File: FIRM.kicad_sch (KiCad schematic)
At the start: 111 parts, among them J1 Conn_01x02_Pin, J2 DM3CS-SF, Q2 IRLML6402, U1 STM32F405RGTx, U2 MIC5219-3.3YM5, U6 A-USBC-20F0-EA-GSR05, U7 W25Q128JVS, U8 ADXL371, U9 INA219AxDCN, X2 32.768khz, Y1 12 MHz

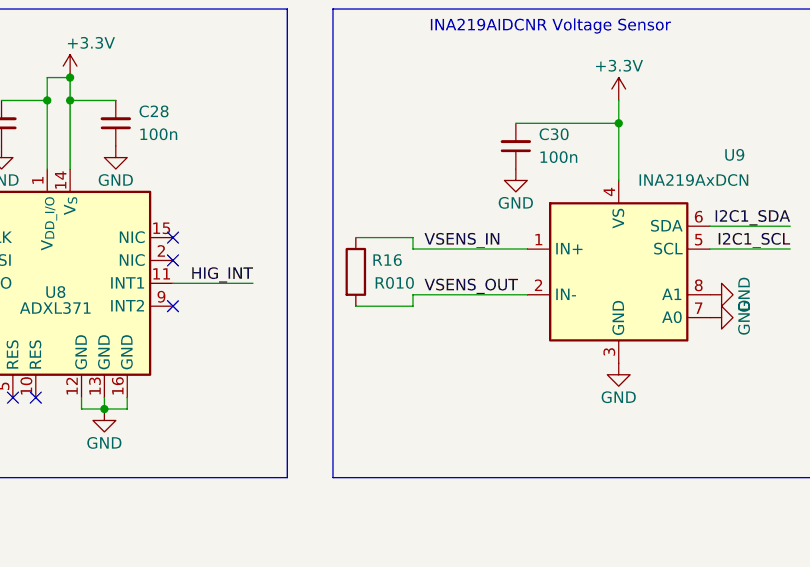
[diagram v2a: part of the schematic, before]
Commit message: Made components 0402s
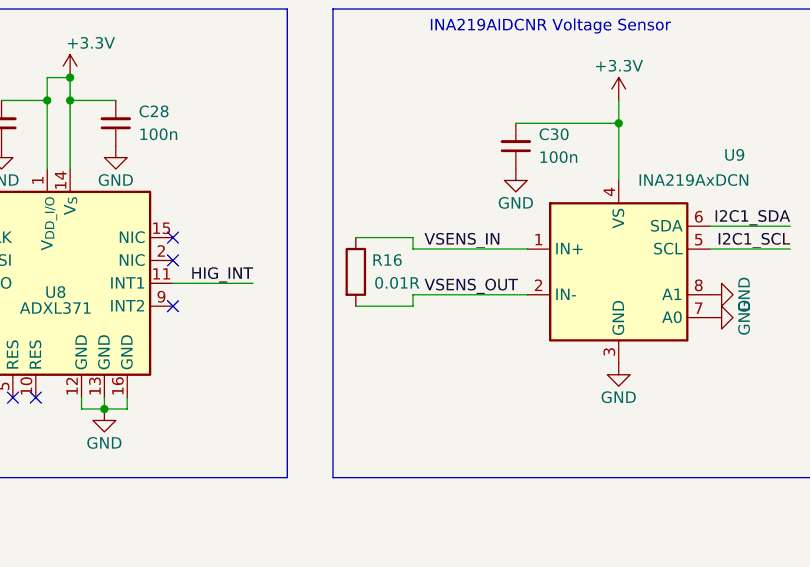
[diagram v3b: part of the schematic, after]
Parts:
- C1, C10, C11, C12, C13, C14, C15, C16, C17, C18, C19, C2, C20, C21, C22, C23, C24, C25, C26, C27, C28, C29, C3, C30, C4, C5, C6, C7, C8, C9: footprint Capacitor_SMD:C_0603_1608Metric -> Capacitor_SMD:C_0402_1005Metric
- D2, D3, D4, D5: footprint LED_SMD:LED_0805_2012Metric -> LED_SMD:LED_0402_1005Metric
- R1, R10, R11, R12, R13, R14, R15, R18, R19, R2, R20, R21, R22, R3, R4, R5, R6, R7, R8, R9: footprint Resistor_SMD:R_0603_1608Metric -> Resistor_SMD:R_0402_1005Metric
- R16: value R010 -> 0.01R; footprint (none) -> Resistor_SMD:R_0402_1005Metric
- U5: footprint Package_LGA:ST_HLGA-10_2x2mm_P0.5mm_LayoutBorder3x2y -> sensors:BMPFootprintNoSolderMask
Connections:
- new net: U8.10 (RES), U8.13 (GND), U8.16 (GND)
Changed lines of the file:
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@@
 			)
 		)
-		(property "Footprint" "Capacitor_SMD:C_0603_1608Metric"
+		(property "Footprint" "Capacitor_SMD:C_0402_1005Metric"
 			(at 88.5952 45.72 0)
 			(effects
@@
 			)
 		)
-		(property "Footprint" "Capacitor_SMD:C_0603_1608Metric"
+		(property "Footprint" "Capacitor_SMD:C_0402_1005Metric"
 			(at 37.7952 45.72 0)
 			(effects
@@
 			)
 		)
-		(property "Footprint" "Resistor_SMD:R_0603_1608Metric"
+		(property "Footprint" "Resistor_SMD:R_0402_1005Metric"
 			(at 21.082 255.27 90)
 			(effects
@@
 			)
 		)
-		(property "Footprint" "Resistor_SMD:R_0603_1608Metric"
+		(property "Footprint" "Resistor_SMD:R_0402_1005Metric"
 			(at 28.702 66.04 90)
 			(effects
@@
 			)
 		)
-		(property "Footprint" "Capacitor_SMD:C_0603_1608Metric"
+		(property "Footprint" "Capacitor_SMD:C_0402_1005Metric"
 			(at 340.36 224.79 0)
 			(effects
@@
 			)
 		)
-		(property "Footprint" "Capacitor_SMD:C_0603_1608Metric"
+		(property "Footprint" "Capacitor_SMD:C_0402_1005Metric"
 			(at 20.0152 64.77 0)
 			(effects
@@
 			)
 		)
-		(property "Footprint" "Capacitor_SMD:C_0603_1608Metric"
+		(property "Footprint" "Capacitor_SMD:C_0402_1005Metric"
 			(at 285.75 105.41 0)
 			(effects
@@
 			)
 		)
-		(property "Footprint" "Resistor_SMD:R_0603_1608Metric"
+		(property "Footprint" "Resistor_SMD:R_0402_1005Metric"
 			(at 52.07 177.8 0)
 			(effects
@@
 			)
 		)
-		(property "Footprint" "LED_SMD:LED_0805_2012Metric"
+		(property "Footprint" "LED_SMD:LED_0402_1005Metric"
 			(at 191.77 116.84 0)
 			(effects
@@
 			)
 		)
-		(property "Footprint" "Capacitor_SMD:C_0603_1608Metric"
+		(property "Footprint" "Capacitor_SMD:C_0402_1005Metric"
 			(at 64.77 195.58 0)
 			(effects
@@
 			)
 		)
-		(property "Footprint" "Resistor_SMD:R_0603_1608Metric"
+		(property "Footprint" "Resistor_SMD:R_0402_1005Metric"
 			(at 59.69 177.8 0)
 			(effects
@@
 			)
 		)
-		(property "Footprint" "Resistor_SMD:R_0603_1608Metric"
+		(property "Footprint" "Resistor_SMD:R_0402_1005Metric"
 			(at 25.4 177.8 0)
 			(effects
@@
 			)
 		)
-		(property "Footprint" "Resistor_SMD:R_0603_1608Metric"
+		(property "Footprint" "Resistor_SMD:R_0402_1005Metric"
 			(at 153.67 111.76 0)
 			(effects
@@
 			)
 		)
-		(property "Footprint" "Resistor_SMD:R_0603_1608Metric"
+		(property "Footprint" "Resistor_SMD:R_0402_1005Metric"
 			(at 38.1 212.09 0)
 			(effects
@@
 			)
 		)
-		(property "Footprint" "Capacitor_SMD:C_0603_1608Metric"
+		(property "Footprint" "Capacitor_SMD:C_0402_1005Metric"
 			(at 66.04 240.03 0)
 			(effects
@@
 			)
 		)
-		(property "Footprint" "Capacitor_SMD:C_0603_1608Metric"
+		(property "Footprint" "Capacitor_SMD:C_0402_1005Metric"
 			(at 228.6 102.87 0)
 			(effects
@@
 			)
 		)
-		(property "Footprint" "Capacitor_SMD:C_0603_1608Metric"
+		(property "Footprint" "Capacitor_SMD:C_0402_1005Metric"
 			(at 42.8752 92.71 0)
 			(effects
@@
 			)
 		)
-		(property "Footprint" "Capacitor_SMD:C_0603_1608Metric"
+		(property "Footprint" "Capacitor_SMD:C_0402_1005Metric"
 			(at 143.2052 45.72 0)
 			(effects
@@
 			)
 		)
-		(property "Footprint" "LED_SMD:LED_0805_2012Metric"
+		(property "Footprint" "LED_SMD:LED_0402_1005Metric"
 			(at 191.77 128.27 0)
 			(effects
@@
 			)
 		)
-		(property "Footprint" "Resistor_SMD:R_0603_1608Metric"
+		(property "Footprint" "Resistor_SMD:R_0402_1005Metric"
 			(at 177.8 105.41 0)
 			(effects
@@
 			)
 		)
-		(property "Footprint" "Resistor_SMD:R_0603_1608Metric"
+		(property "Footprint" "Resistor_SMD:R_0402_1005Metric"
 			(at 144.78 111.76 0)
 			(effects
@@
 			)
 		)
-		(property "Footprint" "Capacitor_SMD:C_0603_1608Metric"
+		(property "Footprint" "Capacitor_SMD:C_0402_1005Metric"
 			(at 64.4652 93.98 0)
 			(effects
@@
 			)
 		)
-		(property "Footprint" "Resistor_SMD:R_0603_1608Metric"
+		(property "Footprint" "Resistor_SMD:R_0402_1005Metric"
 			(at 322.58 208.28 0)
 			(effects
@@
 			)
 		)
-		(property "Footprint" "Resistor_SMD:R_0603_1608Metric"
+		(property "Footprint" "Resistor_SMD:R_0402_1005Metric"
 			(at 177.8 128.27 0)
 			(effects
@@
 			)
 		)
-		(property "Footprint" "Capacitor_SMD:C_0603_1608Metric"
+		(property "Footprint" "Capacitor_SMD:C_0402_1005Metric"
 			(at 40.3352 134.62 0)
 			(effects
@@
 			)
 		)
-		(property "Footprint" "Resistor_SMD:R_0603_1608Metric"
+		(property "Footprint" "Resistor_SMD:R_0402_1005Metric"
 			(at 44.45 177.8 0)
 			(effects
@@
 			)
 		)
-		(property "Footprint" "Capacitor_SMD:C_0603_1608Metric"
+		(property "Footprint" "Capacitor_SMD:C_0402_1005Metric"
 			(at 353.06 138.43 0)
 			(effects
@@
 			)
 		)
-		(property "Footprint" "Resistor_SMD:R_0603_1608Metric"
+		(property "Footprint" "Resistor_SMD:R_0402_1005Metric"
 			(at 379.73 40.64 0)
 			(effects
@@
 			)
 		)
-		(property "Footprint" "Resistor_SMD:R_0603_1608Metric"
+		(property "Footprint" "Resistor_SMD:R_0402_1005Metric"
 			(at 37.592 245.11 90)
 			(effects
@@
 			)
 		)
-		(property "Footprint" "Capacitor_SMD:C_0603_1608Metric"
+		(property "Footprint" "Capacitor_SMD:C_0402_1005Metric"
 			(at 74.6252 134.62 0)
 			(effects
@@
 			)
 		)
-		(property "Footprint" "Capacitor_SMD:C_0603_1608Metric"
+		(property "Footprint" "Capacitor_SMD:C_0402_1005Metric"
 			(at 173.6852 45.72 0)
 			(effects
@@
 			)
 		)
-		(property "Footprint" "Capacitor_SMD:C_0603_1608Metric"
+		(property "Footprint" "Capacitor_SMD:C_0402_1005Metric"
 			(at 327.66 27.94 0)
 			(effects
@@
 			)
 		)
-		(property "Footprint" "Capacitor_SMD:C_0603_1608Metric"
+		(property "Footprint" "Capacitor_SMD:C_0402_1005Metric"
 			(at 131.7752 45.72 0)
 			(effects
@@
 			)
 		)
-		(property "Footprint" "Capacitor_SMD:C_0603_1608Metric"
+		(property "Footprint" "Capacitor_SMD:C_0402_1005Metric"
 			(at 51.7652 134.62 0)
 			(effects
@@
 			)
 		)
-		(property "Footprint" "Resistor_SMD:R_0603_1608Metric"
+		(property "Footprint" "Resistor_SMD:R_0402_1005Metric"
 			(at 242.062 222.25 90)
 			(effects
@@
 			)
 		)
-		(property "Footprint" "LED_SMD:LED_0805_2012Metric"
+		(property "Footprint" "LED_SMD:LED_0402_1005Metric"
 			(at 326.39 201.93 0)
 			(effects
@@
 			)
 		)
-		(property "Footprint" "Capacitor_SMD:C_0603_1608Metric"
+		(property "Footprint" "Capacitor_SMD:C_0402_1005Metric"
 			(at 49.2252 45.72 0)
 			(effects
@@
 			)
 		)
-		(property "Footprint" "Capacitor_SMD:C_0603_1608Metric"
+		(property "Footprint" "Capacitor_SMD:C_0402_1005Metric"
 			(at 261.62 224.79 0)
 			(effects
@@
 			)
 		)
-		(property "Footprint" "Resistor_SMD:R_0603_1608Metric"
+		(property "Footprint" "Resistor_SMD:R_0402_1005Metric"
 			(at 33.02 177.8 0)
 			(effects
@@
 			)
 		)
-		(property "Footprint" "Package_LGA:ST_HLGA-10_2x2mm_P0.5mm_LayoutBorder3x2y"
+		(property "Footprint" "sensors:BMPFootprintNoSolderMask"
 			(at 326.898 27.432 0)
 			(effects
@@
 			)
 		)
-		(property "Footprint" "LED_SMD:LED_0805_2012Metric"
+		(property "Footprint" "LED_SMD:LED_0402_1005Metric"
 			(at 191.77 105.41 0)
 			(effects
@@
 			)
 		)
-		(property "Footprint" "Capacitor_SMD:C_0603_1608Metric"
+		(property "Footprint" "Capacitor_SMD:C_0402_1005Metric"
 			(at 320.04 27.94 0)
 			(effects
@@
 			)
 		)
-		(property "Footprint" "Capacitor_SMD:C_0603_1608Metric"
+		(property "Footprint" "Capacitor_SMD:C_0402_1005Metric"
 			(at 241.3 102.87 0)
 			(effects
@@
 			)
 		)
-		(property "Footprint" "Resistor_SMD:R_0603_1608Metric"
+		(property "Footprint" "Resistor_SMD:R_0402_1005Metric"
 			(at 394.97 194.818 90)
 			(effects
@@
 			)
 		)
-		(property "Footprint" "Resistor_SMD:R_0603_1608Metric"
+		(property "Footprint" "Resistor_SMD:R_0402_1005Metric"
 			(at 388.62 192.278 90)
 			(effects
@@
 			)
 		)
-		(property "Footprint" "Capacitor_SMD:C_0603_1608Metric"
+		(property "Footprint" "Capacitor_SMD:C_0402_1005Metric"
 			(at 350.52 148.59 0)
 			(effects
@@
 			)
 		)
-		(property "Value" "R010"
+		(property "Value" "0.01R"
 			(at 270.002 120.65 0)
 			(effects
@@
 			)
 		)
-		(property "Footprint" ""
+		(property "Footprint" "Resistor_SMD:R_0402_1005Metric"
 			(at 266.192 119.38 90)
 			(effects
@@
 			)
 		)
-		(property "Footprint" "Capacitor_SMD:C_0603_1608Metric"
+		(property "Footprint" "Capacitor_SMD:C_0402_1005Metric"
 			(at 74.6252 45.72 0)
 			(effects
@@
 			)
 		)
-		(property "Footprint" "Capacitor_SMD:C_0603_1608Metric"
+		(property "Footprint" "Capacitor_SMD:C_0402_1005Metric"
 			(at 23.8252 45.72 0)
 			(effects
@@
 			)
 		)
-		(property "Footprint" "Resistor_SMD:R_0603_1608Metric"
+		(property "Footprint" "Resistor_SMD:R_0402_1005Metric"
 			(at 177.8 116.84 0)
 			(effects
@@
 			)
 		)
-		(property "Footprint" "Capacitor_SMD:C_0603_1608Metric"
+		(property "Footprint" "Capacitor_SMD:C_0402_1005Metric"
 			(at 254 76.2 0)
 			(effects
@@
 			)
 		)
-		(property "Footprint" "Capacitor_SMD:C_0603_1608Metric"
+		(property "Footprint" "Capacitor_SMD:C_0402_1005Metric"
 			(at 63.1952 134.62 0)
 			(effects
@@
 			)
 		)
-		(property "Footprint" "Capacitor_SMD:C_0603_1608Metric"
+		(property "Footprint" "Capacitor_SMD:C_0402_1005Metric"
 			(at 61.9252 45.72 0)
 			(effects
@@
 			)
 		)
-		(property "Footprint" "Resistor_SMD:R_0603_1608Metric"
+		(property "Footprint" "Resistor_SMD:R_0402_1005Metric"
 			(at 31.242 255.27 90)
 			(effects
@@
 			)
 		)
-		(property "Footprint" "Capacitor_SMD:C_0603_1608Metric"
+		(property "Footprint" "Capacitor_SMD:C_0402_1005Metric"
 			(at 322.58 222.25 0)
 			(effects
@@
 			)
 		)
-		(property "Footprint" "Capacitor_SMD:C_0603_1608Metric"
+		(property "Footprint" "Capacitor_SMD:C_0402_1005Metric"
 			(at 264.16 76.2 0)
 			(effects

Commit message: Assign footprint using local libraries
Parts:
- J2: footprint DM3CS-SF:HRS_DM3CS-SF -> connectors:HRS_DM3CS-SF
- U3: footprint ICM-45686:IC_ICM-45686 -> sensors:IC_ICM-45686
- U4: footprint MMC5983MA:PQFN50P300X300X100-16N -> sensors:IC_MMC5983MA
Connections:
- new net: U8.10 (RES), U8.13 (GND), U8.16 (GND)
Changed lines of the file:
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@@
 			)
 		)
-		(property "Footprint" "MMC5983MA:PQFN50P300X300X100-16N"
+		(property "Footprint" "sensors:IC_MMC5983MA"
 			(at 379.984 122.428 0)
 			(effects
@@
 			)
 		)
-		(property "Footprint" "ICM-45686:IC_ICM-45686"
+		(property "Footprint" "sensors:IC_ICM-45686"
 			(at 274.828 68.58 0)
 			(effects
@@
 		(on_board yes)
 		(dnp no)
-		(fields_autoplaced yes)
 		(property "Reference" "J2"
 			(at 96.52 171.45 0)
@@
 			)
 		)
-		(property "Footprint" "DM3CS-SF:HRS_DM3CS-SF"
+		(property "Footprint" "connectors:HRS_DM3CS-SF"
 			(at 96.52 176.53 0)
 			(effects

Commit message: Make changes to test points, pads, usb-c, jlcpcb settings
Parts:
- removed TP1: GND Through-Hole, TestPoint:TestPoint_THTPad_1.5x1.5mm_Drill0.7mm, symbol Connector:TestPoint
- removed TP12: PA15 Test Point, connectors:Testpoint_1.5x1.5mm_1.0mm, symbol Connector:TestPoint
- removed TP13: PB3 Test Point, connectors:Testpoint_1.5x1.5mm_1.0mm, symbol Connector:TestPoint
- removed TP14: PB4 Test Point, connectors:Testpoint_1.5x1.5mm_1.0mm, symbol Connector:TestPoint
- removed TP15: PB5 Test Point, connectors:Testpoint_1.5x1.5mm_1.0mm, symbol Connector:TestPoint
- removed TP17: PB10 Test Point, connectors:Testpoint_1.5x1.5mm_1.0mm, symbol Connector:TestPoint
- removed TP18: PB11 Test Point, connectors:Testpoint_1.5x1.5mm_1.0mm, symbol Connector:TestPoint
- removed TP24: PC13 Test Point, connectors:Testpoint_1.5x1.5mm_1.0mm, symbol Connector:TestPoint
- removed TP27: GND Test Point, connectors:Testpoint_1.5x1.5mm_1.0mm, symbol Connector:TestPoint
- removed TP29: PC0 Test Point, connectors:Testpoint_1.5x1.5mm_1.0mm, symbol Connector:TestPoint
- removed TP30: PC6 Test Point, connectors:Testpoint_1.5x1.5mm_1.0mm, symbol Connector:TestPoint
- removed TP7: PA3 Test Point, connectors:Testpoint_1.5x1.5mm_1.0mm, symbol Connector:TestPoint
- J2: renamed from J1; footprint Connector_PinHeader_2.54mm:PinHeader_1x02_P2.54mm_Vertical -> connectors:power_headers
- TP10: renamed from TP20; footprint TestPoint:TestPoint_Pad_1.0x1.0mm -> connectors:smd_test_pads_1mm
- TP11: renamed from TP21; footprint TestPoint:TestPoint_Pad_1.0x1.0mm -> connectors:smd_test_pads_1mm
- TP12: renamed from TP2; footprint TestPoint:TestPoint_THTPad_1.5x1.5mm_Drill0.7mm -> connectors:Testpoint_1.5x1.5mm_1.0mm
- TP13: renamed from TP3; footprint TestPoint:TestPoint_THTPad_1.5x1.5mm_Drill0.7mm -> connectors:Testpoint_1.5x1.5mm_1.0mm
- TP16: renamed from TP22; footprint TestPoint:TestPoint_Pad_1.0x1.0mm -> connectors:smd_test_pads_1mm
- TP17: renamed from TP23; footprint TestPoint:TestPoint_Pad_1.0x1.0mm -> connectors:smd_test_pads_1mm
- TP18: renamed from TP31; footprint TestPoint:TestPoint_Pad_1.0x1.0mm -> connectors:smd_test_pads_1mm
- TP19: renamed from TP32; footprint TestPoint:TestPoint_Pad_1.0x1.0mm -> connectors:smd_test_pads_1mm
- TP20: renamed from TP33; footprint TestPoint:TestPoint_Pad_1.0x1.0mm -> connectors:smd_test_pads_1mm
- TP21: renamed from TP35; footprint TestPoint:TestPoint_Pad_1.0x1.0mm -> connectors:smd_test_pads_1mm
- TP22: renamed from TP36; footprint TestPoint:TestPoint_Pad_1.0x1.0mm -> connectors:smd_test_pads_1mm
- TP23: renamed from TP37; footprint TestPoint:TestPoint_Pad_1.0x1.0mm -> connectors:smd_test_pads_1mm
- TP24: renamed from TP38; footprint TestPoint:TestPoint_Pad_1.0x1.0mm -> connectors:smd_test_pads_1mm
- TP25: footprint TestPoint:TestPoint_Pad_1.0x1.0mm -> connectors:smd_test_pads_1mm
- TP6: renamed from TP8; footprint TestPoint:TestPoint_Pad_1.0x1.0mm -> connectors:smd_test_pads_1mm
- TP7: renamed from TP9; footprint TestPoint:TestPoint_Pad_1.0x1.0mm -> connectors:smd_test_pads_1mm
- TP8: renamed from TP16; footprint TestPoint:TestPoint_Pad_1.0x1.0mm -> connectors:smd_test_pads_1mm
- TP9: renamed from TP19; footprint TestPoint:TestPoint_Pad_1.0x1.0mm -> connectors:smd_test_pads_1mm
- renumbered C15 to C1, C14 to C10, C21 to C11, C27 to C12, C2 to C13, C10 to C14, C1 to C15, C7 to C16, C8 to C17, C16 to C18, C29 to C19, C6 to C2, C28 to C20, C25 to C21, C20 to C22, C30 to C23, C22 to C24, C19 to C25, C23 to C26, C26 to C27, C24 to C28, C18 to C29, C5 to C3, C17 to C30, C11 to C4, C13 to C5, C4 to C6, C12 to C7, C3 to C8, D2 to D1, D3 to D2, D4 to D3, D1 to D4, H3 to H1, H1 to H3, J2 to J1, Q2 to Q1, R13 to R1, R2 to R10, R18 to R11, R19 to R12, R10 to R13, R11 to R14, R12 to R15, R8 to R16, R16 to R17, R15 to R18, R20 to R19, R6 to R2, R9 to R20, R22 to R21, R1 to R3, R5 to R4, R14 to R5, R7 to R6, R21 to R7, R4 to R8, R3 to R9, TP4 to TP1, TP28 to TP14, TP26 to TP15, TP5 to TP2, TP6 to TP3, TP10 to TP4, TP11 to TP5, U7 to U1, U1 to U2, U8 to U3, U3 to U4, U9 to U5, U2 to U6, U5 to U7, U4 to U8, U6 to U9, X2 to X1
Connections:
- net VSENS_IN: no longer C24.1
- net VSENS_OUT: now also C24.1
- new net: U3.10 (RES), U3.13 (GND), U3.16 (GND)
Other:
- moved on the sheet: C24, TP10, TP11, TP14, TP15, TP4, TP5, TP6, TP7, TP8, TP9

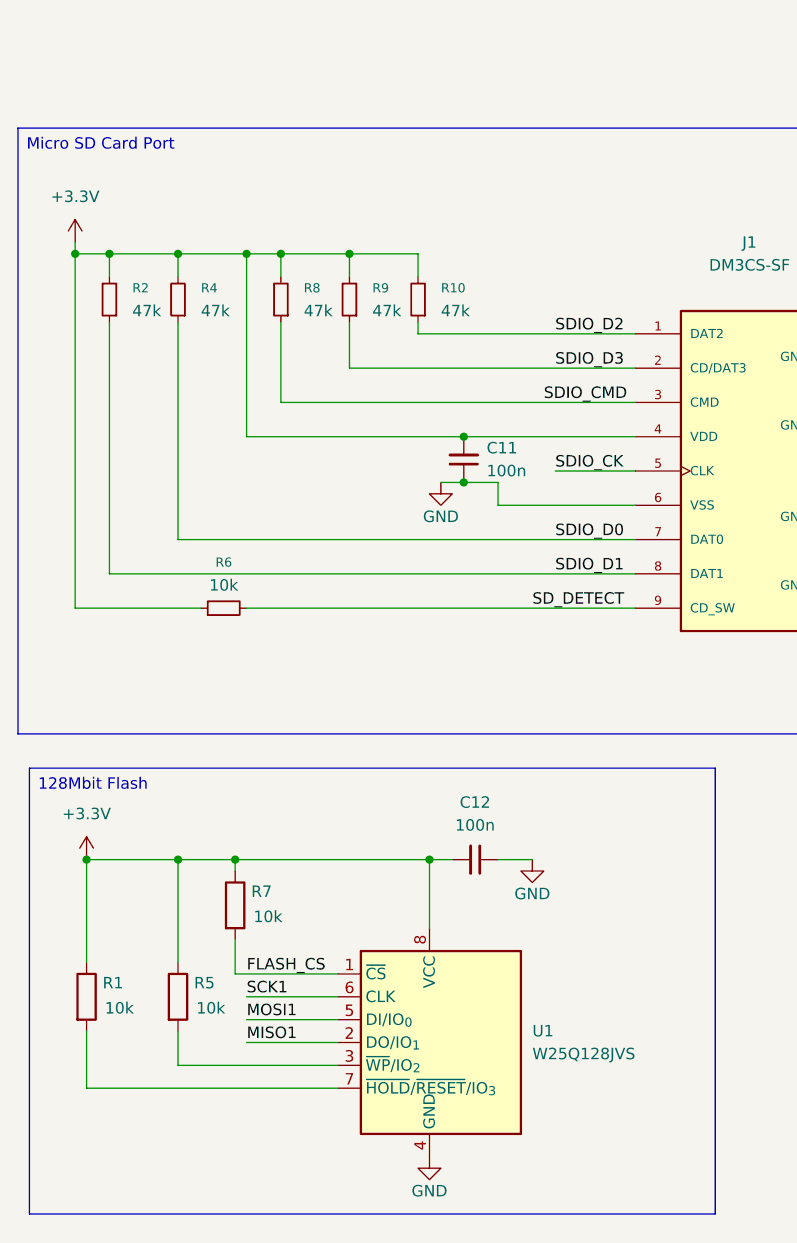
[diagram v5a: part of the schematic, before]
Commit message: need footprints
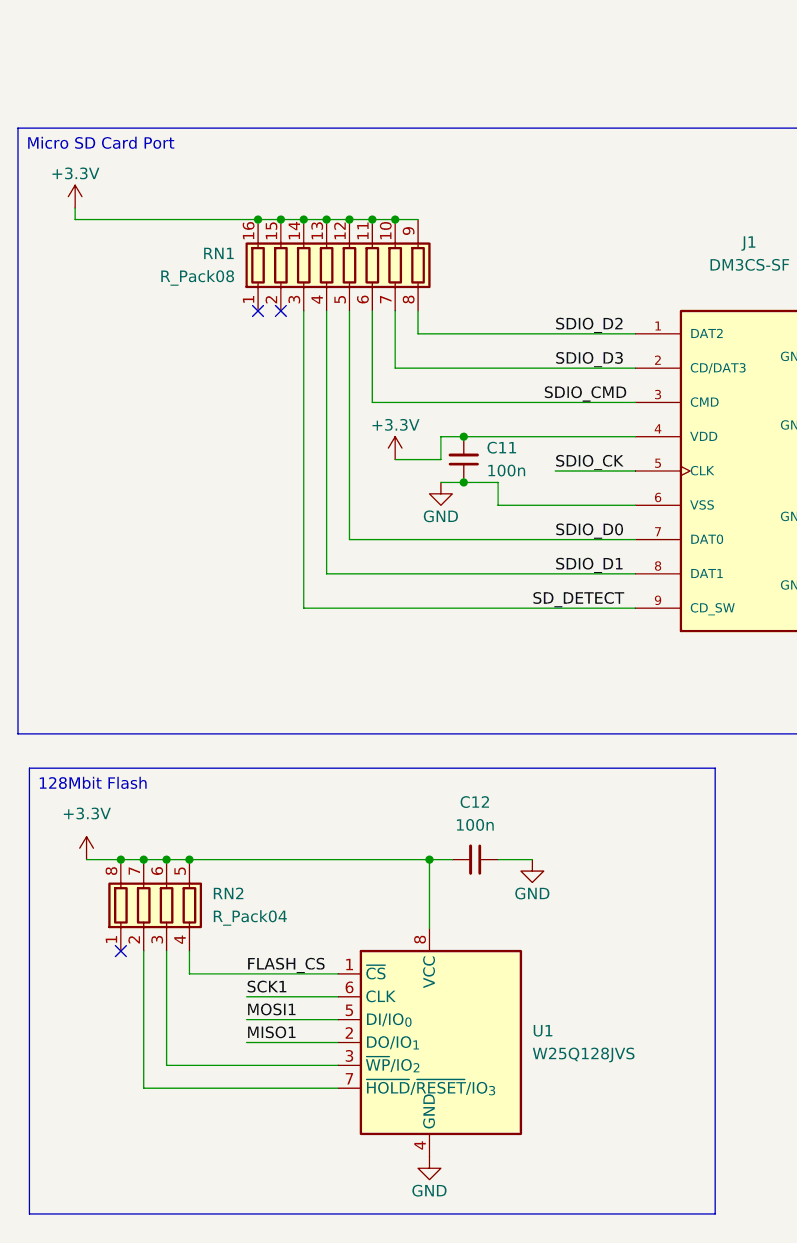
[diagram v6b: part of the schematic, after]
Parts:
- removed R1, R5, R7: 10k, Resistor_SMD:R_0402_1005Metric, symbol Device:R
- removed R10, R2, R4, R8, R9: 47k, Resistor_SMD:R_0402_1005Metric, symbol Device:R_Small
- removed R6: 10k, Resistor_SMD:R_0402_1005Metric, symbol Device:R_Small
- added RN1: R_Pack08, Resistor_SMD:R_Array_Convex_8x0602, symbol Device:R_Pack08
- added RN2: R_Pack04, symbol Device:R_Pack04
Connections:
- net +3.3V: now also RN1.10 (R7.2), RN1.11 (R6.2), RN1.12 (R5.2), RN1.13 (R4.2), RN1.14 (R3.2), RN1.15 (R2.2), RN1.16 (R1.2), RN1.9 (R8.2), RN2.5 (R4.2), RN2.6 (R3.2), RN2.7 (R2.2), RN2.8 (R1.2)
- net FLASH_CS: now also RN2.4 (R4.1)
- net SDIO_CMD: now also RN1.6 (R6.1)
- net SDIO_D0: now also RN1.5 (R5.1)
- net SDIO_D1: now also RN1.4 (R4.1)
- net SDIO_D2: now also RN1.8 (R8.1)
- net SDIO_D3: now also RN1.7 (R7.1)
- net SD_DETECT: now also RN1.3 (R3.1)
- net at U1.7 (~{HOLD}/~{RESET}/IO_{3}): now also RN2.2 (R2.1)
- net at U1.3 (~{WP}/IO_{2}): now also RN2.3 (R3.1)
- new net: U3.10 (RES), U3.13 (GND), U3.16 (GND)
- no-connect marks 20 -> 23
